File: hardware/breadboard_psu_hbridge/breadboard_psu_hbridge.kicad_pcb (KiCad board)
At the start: 2 copper layers, 51.7 x 45.7 mm, 52 parts, among them J1 USB_B_Micro, J2 Conn_01x02, J3 Conn_01x02, U1 74LS132, U2 LM4871MX_NOPB, U3 LM2733YMF, U4 ZXBM5210-S

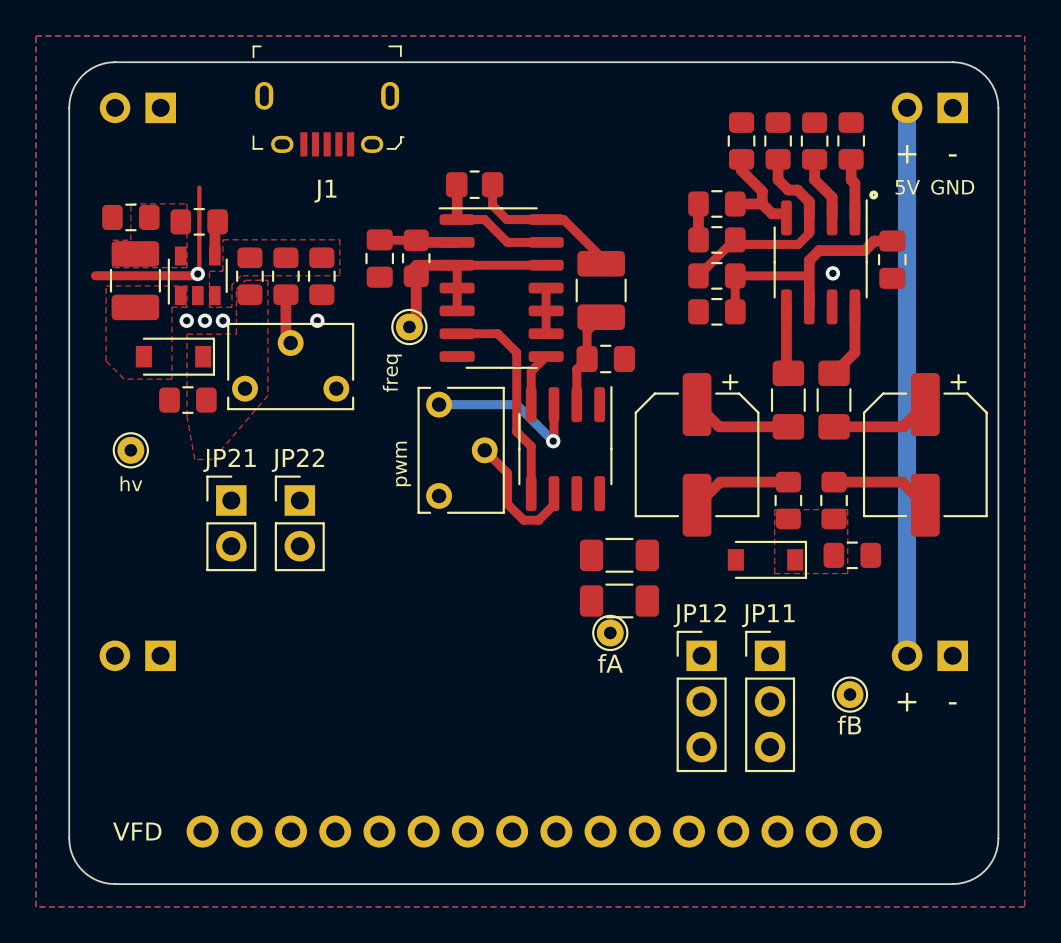
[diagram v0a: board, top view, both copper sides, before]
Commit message: hw: finished h-bridge psu test board
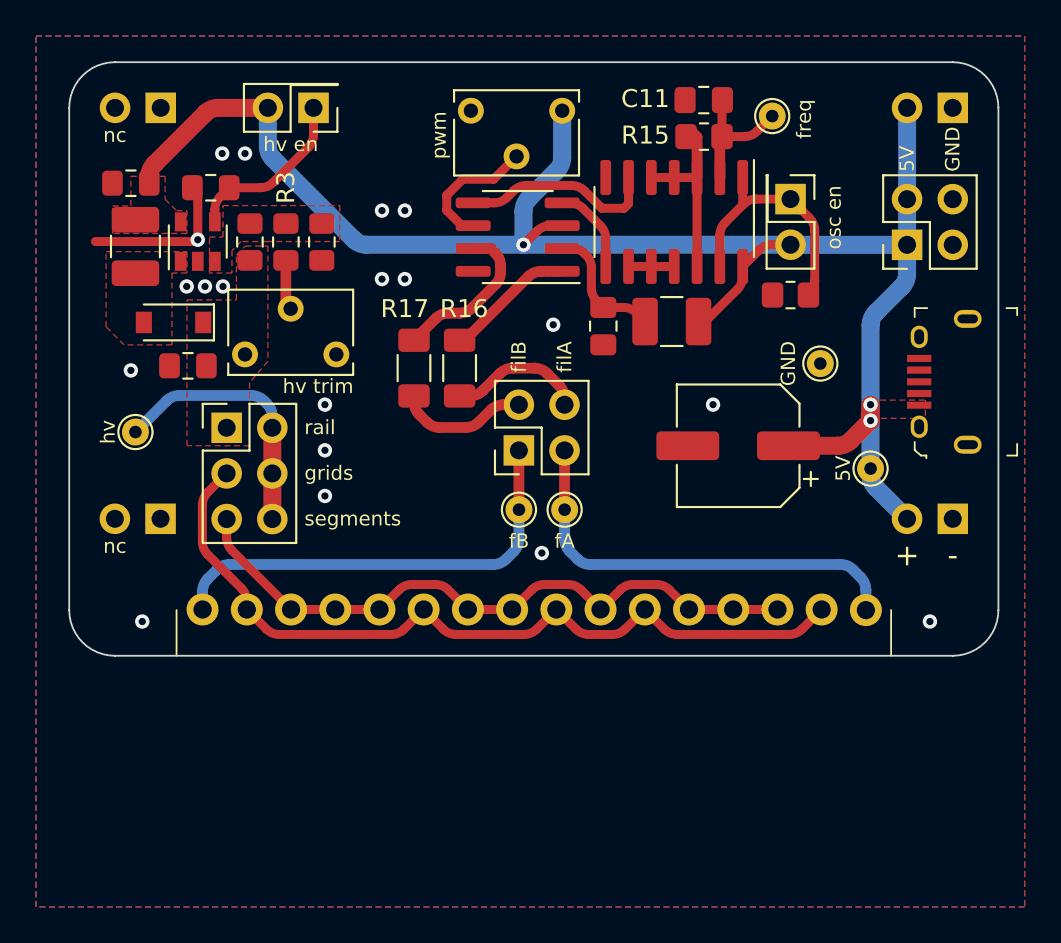
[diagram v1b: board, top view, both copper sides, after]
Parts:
- removed C10, C5: 1µF, Capacitor_SMD:C_0805_2012Metric_Pad1.15x1.40mm_HandSolder
- removed C6: 10µF, Capacitor_SMD:C_0805_2012Metric_Pad1.18x1.45mm_HandSolder
- removed C7, C8: 47µF, Capacitor_SMD:CP_Elec_6.3x5.9
- removed C9: 100nF, Capacitor_SMD:C_0805_2012Metric_Pad1.15x1.40mm_HandSolder
- removed D2: 3.3V, Diode_SMD:D_SOD-123
- removed JP11, JP12: Jumper_3_Bridged12, Connector_PinHeader_2.54mm:PinHeader_1x03_P2.54mm_Vertical
- removed JP21, JP22: Jumper_2_Bridged, Connector_PinHeader_2.54mm:PinHeader_1x02_P2.54mm_Vertical
- removed R10, R11: 12Ω 0.25W, Resistor_SMD:R_1206_3216Metric_Pad1.42x1.75mm_HandSolder
- removed R12, R13: 220Ω, Resistor_SMD:R_0805_2012Metric_Pad1.15x1.40mm_HandSolder
- removed R5, R6, R7, R9: 10kΩ, Resistor_SMD:R_0805_2012Metric_Pad1.15x1.40mm_HandSolder
- removed R8: 2.2kΩ, Resistor_SMD:R_0805_2012Metric_Pad1.15x1.40mm_HandSolder
- removed REF** (x2): PinHeader_1x02_P2.54mm_Vertical, Connector_PinHeader_2.54mm:PinHeader_1x02_P2.54mm_Vertical
- removed U2: LM4871MX_NOPB, Package_SO:SOIC-8_3.9x4.9mm_P1.27mm
- removed VFD: IVL2-7_5-singleSide, extra_libraries:IVL2-7_5-singleSide
- added A1: 2021, extra:AHOI, B.Cu at (127.8, 64.8)
- added J2: PWR Header, Connector_PinHeader_2.54mm:PinHeader_2x02_P2.54mm_Vertical, F.Cu at (137.3, 50.2)
- added J3: HV Jumper, Connector_PinHeader_2.54mm:PinHeader_2x03_P2.54mm_Vertical, F.Cu at (99.5, 60.3)
- added J31: Breadboard NC, Connector_PinHeader_2.54mm:PinHeader_1x02_P2.54mm_Vertical, B.Cu at (95.8, 42.5)
- added J32: Breadboard NC, Connector_PinHeader_2.54mm:PinHeader_1x02_P2.54mm_Vertical, B.Cu at (95.8, 65.4)
- added J4: Filament Jumper, Connector_PinHeader_2.54mm:PinHeader_2x02_P2.54mm_Vertical, F.Cu at (115.7, 61.6)
- added J5: Filament EN, Connector_PinHeader_2.54mm:PinHeader_2x01_P2.54mm_Vertical, F.Cu at (130.8, 47.6)
- added J6: HV EN, Connector_PinHeader_2.54mm:PinHeader_2x01_P2.54mm_Vertical, F.Cu at (104.3, 42.5)
- added TP1: 5V, TestPoint:TestPoint_THTPad_D1.5mm_Drill0.7mm, F.Cu at (135.3, 62.6)
- added TP4: GND, TestPoint:TestPoint_THTPad_D1.5mm_Drill0.7mm, F.Cu at (132.5, 56.8)
- added VFD1: IVL2-5_7, extra:IVL2-7_5-singleSide, F.Cu at (155.8, 102.5)
- C4: value 10nF -> 47µF; footprint Capacitor_SMD:C_0805_2012Metric_Pad1.15x1.40mm_HandSolder -> Capacitor_SMD:CP_Elec_6.3x5.9
- J21: renamed from J3; value Conn_01x02 -> Breadboard Rail
- J22: renamed from J2; value Conn_01x02 -> Breadboard Rail
- R14: value 2.7kΩ -> 10kΩ
- moved J1 35.5 mm to (138.0, 57.8), turned to 90 degrees
- moved TP3 23.3 mm to (129.8, 43.0), turned to 90 degrees
- moved TP11 21.1 mm to (115.7, 64.9)
- moved C11 20.1 mm to (126.0, 42.1), turned to 180 degrees
- moved R14 18.6 mm to (130.8, 53.0)
- moved RV1 17.7 mm to (118.1, 42.7), turned to 0 degrees
- moved R15 17.4 mm to (126.0, 44.1), turned to 180 degrees
- moved R17 17.3 mm to (109.9, 57.0), turned to 90 degrees
- moved C4 17.0 mm to (127.9, 61.3), turned to 180 degrees
- moved R16 13.7 mm to (112.4, 57.0), turned to 90 degrees
- moved U4 12.1 mm to (115.6, 49.7), turned to 180 degrees
- moved U1 10.3 mm to (124.3, 48.9), turned to -90 degrees
- moved J21 7.62 mm to (139.8, 65.4)
- moved TP12 7.31 mm to (118.3, 64.9)
- moved L2 4.29 mm to (124.2, 54.4), turned to 180 degrees
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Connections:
- C4 pad 1: Net-(C4-Pad1) -> /5V
- J1 pad 2: Net-(J1-Pad2) -> unconnected-(J1-Pad2)
- J1 pad 3: Net-(J1-Pad3) -> unconnected-(J1-Pad3)
- J1 pad 4: Net-(J1-Pad4) -> unconnected-(J1-Pad4)
- R1 pad 1: /5V -> Net-(U3-Pad4)
- R1 pad 2: /~{HV_SHDN} -> GND
- R14 pad 1: /5V -> /H_EN
- R14 pad 2: /H_SHDN -> GND
- R15 pad 2: Net-(R15-Pad2) -> Net-(U1-Pad12)
- TP2 pad 1: /HV -> /HV_Jumper
- TP3 pad 1: Net-(R15-Pad2) -> Net-(C11-Pad1)
- U1 pad 1: /H_SHDN -> /H_EN
- U1 pad 12: Net-(R15-Pad2) -> Net-(U1-Pad12)
- U1 pad 13: /H_SHDN -> /H_EN
- U1 pad 3: Net-(R15-Pad2) -> Net-(U1-Pad12)
- U1 pad 4: Net-(R15-Pad2) -> Net-(U1-Pad12)
- U1 pad 5: Net-(R15-Pad2) -> Net-(U1-Pad12)
- U3 pad 4: /~{HV_SHDN} -> Net-(U3-Pad4)
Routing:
- net /HV_Grids: track 0.00 -> 45.2 mm
- net /HV_Segments: track 0.00 -> 36.7 mm
- net /5V: track 62.6 -> 98.0 mm, vias 1 -> 3
- net /FIL_B: track 0.00 -> 25.0 mm
- net /FIL_A: track 0.00 -> 24.3 mm
- net /HV_Jumper: track 0.00 -> 14.7 mm
- net /H_EN: track 0.00 -> 14.1 mm
- net Net-(R15-Pad2): track 13.1 -> 0.00 mm
- net Net-(R5-Pad2): track 12.5 -> 0.00 mm
- net Net-(U1-Pad12): track 0.00 -> 10.1 mm
- net Net-(U3-Pad4): track 0.00 -> 9.72 mm
- net Net-(R17-Pad2): track 0.00 -> 8.95 mm
- net /FIL_H_A: track 0.00 -> 7.58 mm
- net /FIL_H_B: track 0.00 -> 7.33 mm
- net Net-(R16-Pad2): track 0.00 -> 7.25 mm
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- removed copper zone on F.Cu, net Net-(C10-Pad1)
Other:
- board size 51.7 x 45.7 mm -> 51.7 x 33 mm
- board text added: "VFD PSU HB"
- board text added: "filA"
- board text added: "filB"
- board text added: "grids"
- board text added: "hv en"
- board text added: "hv trim"
- board text added: "nc"
- board text added: "osc en"
- board text added: "rail"
- board text added: "segments"
- board text removed: "Breadboard VFD PSU"
- board text removed: "Breadboard VFD PSU v1.0 partly based on a design by rolo 2020 ansemjo"

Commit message: hw: tweak breadboard psu for fabrication
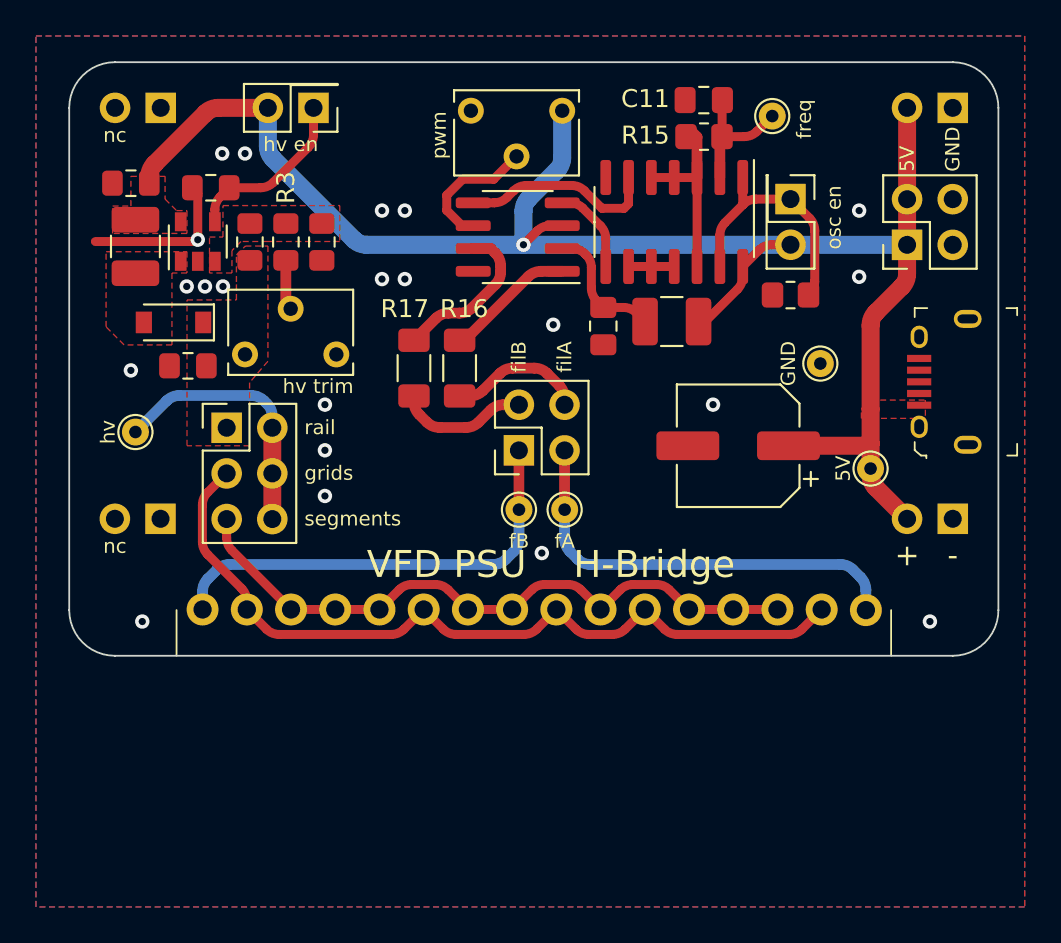
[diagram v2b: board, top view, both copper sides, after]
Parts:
- moved A1 1.87 mm to (127.9, 62.9)
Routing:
- net /5V: track 98.0 -> 96.6 mm, vias 3 -> 1
- net GND: vias 19 -> 21
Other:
- board text added: "JLCJLCJLCJLC"
- board text added: "VFD PSU H-Bridge"
- board text removed: "VFD PSU HB"
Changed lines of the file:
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@@
   (paper "A4")
   (title_block
+    (title "Breadboard VFD PSU")
+    (date "2021-08-28")
     (rev "1")
   )
@@
   )
   (footprint "extra:AHOI" (layer "B.Cu")
-    (at 127.778 64.77 180)
+    (at 127.905 62.9078 180)
     (property "Sheetfile" "breadboard_psu_hbridge.kicad_sch")
     (property "Sheetname" "")
@@
       (effects (font (size 1 1) (thickness 0.15)) (justify mirror))
     )
-    (fp_text user "ansemjo" (at 4.1 2.54) (layer "B.SilkS")
+    (fp_text user "ansemjo" (at 4.1 2.54 180) (layer "B.SilkS")
       (effects (font (size 1 1) (thickness 0.15)) (justify mirror))
     )
@@
   (gr_arc (start 139.843 70.485) (end 139.843 73.025) (angle -90) (layer "Edge.Cuts") (width 0.1))
   (gr_arc (start 139.843 42.545) (end 142.383 42.545) (angle -90) (layer "Edge.Cuts") (width 0.1))
+  (gr_text "JLCJLCJLCJLC" (at 127.905 66.167) (layer "B.SilkS")
+    (effects (font (size 0.8 0.8) (thickness 0.1)) (justify mirror))
+  )
   (gr_text "-" (at 139.843 67.437) (layer "F.SilkS")
     (effects (font (size 1.2 1.2) (thickness 0.3)))
@@
     (effects (font (size 0.8 0.8) (thickness 0.1)))
   )
+  (gr_text "VFD PSU    H-Bridge" (at 117.491 67.945) (layer "F.SilkS")
+    (effects (font (size 1.5 1.5) (thickness 0.3)))
+  )
   (gr_text "hv en" (at 103.013 44.577) (layer "F.SilkS")
     (effects (font (size 0.8 0.8) (thickness 0.1)))
@@
   (gr_text "filA" (at 118.253 57.277 90) (layer "F.SilkS")
     (effects (font (size 0.8 0.8) (thickness 0.1)) (justify left))
-  )
-  (gr_text "VFD PSU HB" (at 127.143 66.675) (layer "F.Mask")
-    (effects (font (size 1.5 1.5) (thickness 0.3)))
   )
   (segment (start 97.846 49.881) (end 97.82099 49.85599) (width 0.25) (layer "F.Cu") (net 1))
@@
   (via (at 138.573 71.12) (size 0.8) (drill 0.4) (layers "F.Cu" "B.Cu") (free) (net 1))
   (via (at 99.203 45.085) (size 0.8) (drill 0.4) (layers "F.Cu" "B.Cu") (free) (net 1))
+  (via (at 134.636 51.943) (size 0.8) (drill 0.4) (layers "F.Cu" "B.Cu") (free) (net 1))
   (via (at 109.363 52.07) (size 0.8) (drill 0.4) (layers "F.Cu" "B.Cu") (free) (net 1))
   (via (at 94.758 71.12) (size 0.8) (drill 0.4) (layers "F.Cu" "B.Cu") (free) (net 1))
@@
   (via (at 117.618 54.61) (size 0.8) (drill 0.4) (layers "F.Cu" "B.Cu") (free) (net 1))
   (via (at 109.363 48.26) (size 0.8) (drill 0.4) (layers "F.Cu" "B.Cu") (free) (net 1))
+  (via (at 134.636 48.26) (size 0.8) (drill 0.4) (layers "F.Cu" "B.Cu") (free) (net 1))
   (via (at 94.123 57.15) (size 0.8) (drill 0.4) (layers "F.Cu" "B.Cu") (free) (net 1))
   (segment (start 102.746 53.454) (end 103.013 53.721) (width 0.6) (layer "F.Cu") (net 3))
@@
   (segment (start 103.013 51.298) (end 102.746 51.031) (width 0.5) (layer "F.Cu") (net 3))
   (segment (start 128.159 51.994256) (end 128.159 51.37) (width 0.5) (layer "F.Cu") (net 5))
-  (segment (start 135.271 59.944) (end 135.271 59.055) (width 1) (layer "F.Cu") (net 5))
   (segment (start 127.866107 52.637893) (end 126.072 54.432) (width 0.5) (layer "F.Cu") (net 5))
   (segment (start 128.159 51.37) (end 128.159 51.930786) (width 0.5) (layer "F.Cu") (net 5))
   (segment (start 98.982214 42.545) (end 101.743 42.545) (width 1) (layer "F.Cu") (net 5))
   (segment (start 126.072 54.432) (end 125.7015 54.432) (width 0.5) (layer "F.Cu") (net 5))
-  (segment (start 130.705 61.341) (end 133.459786 61.341) (width 1) (layer "F.Cu") (net 5))
-  (segment (start 134.166893 61.048107) (end 135.271 59.944) (width 1) (layer "F.Cu") (net 5))
+  (segment (start 135.563893 53.936107) (end 137.010107 52.489893) (width 1) (layer "F.Cu") (net 5))
+  (segment (start 137.303 65.405) (end 135.563893 63.665893) (width 1) (layer "F.Cu") (net 5))
   (segment (start 128.159 51.37) (end 129.076107 50.452893) (width 0.5) (layer "F.Cu") (net 5))
   (segment (start 118.118 49.098) (end 117.438214 49.098) (width 0.5) (layer "F.Cu") (net 5))
+  (segment (start 135.271 62.958786) (end 135.271 61.214) (width 1) (layer "F.Cu") (net 5))
+  (segment (start 137.303 51.782786) (end 137.303 50.165) (width 1) (layer "F.Cu") (net 5))
+  (segment (start 135.271 61.214) (end 135.271 59.309) (width 1) (layer "F.Cu") (net 5))
+  (segment (start 130.705 61.341) (end 135.144 61.341) (width 1) (layer "F.Cu") (net 5))
+  (segment (start 135.144 61.341) (end 135.271 61.214) (width 1) (layer "F.Cu") (net 5))
+  (segment (start 135.271 59.309) (end 135.271 54.643214) (width 1) (layer "F.Cu") (net 5))
   (segment (start 116.731107 49.390893) (end 115.962 50.16) (width 0.5) (layer "F.Cu") (net 5))
   (segment (start 95.440893 45.672107) (end 98.275107 42.837893) (width 1) (layer "F.Cu") (net 5))
   (segment (start 129.783214 50.16) (end 130.818 50.16) (width 0.5) (layer "F.Cu") (net 5))
   (segment (start 95.148 46.736) (end 95.148 46.379214) (width 1) (layer "F.Cu") (net 5))
-  (via (at 135.271 59.055) (size 0.8) (drill 0.4) (layers "F.Cu" "B.Cu") (net 5))
+  (segment (start 137.303 50.165) (end 137.303 42.545) (width 1) (layer "F.Cu") (net 5))
   (via (at 115.962 50.16) (size 0.8) (drill 0.4) (layers "F.Cu" "B.Cu") (net 5))
-  (via (at 135.271 59.944) (size 0.8) (drill 0.4) (layers "F.Cu" "B.Cu") (net 5))
   (arc (start 128.159 51.930786) (mid 128.08288 52.313469) (end 127.866107 52.637893) (width 0.5) (layer "F.Cu") (net 5))
   (arc (start 98.982214 42.545) (mid 98.599531 42.62112) (end 98.275107 42.837893) (width 1) (layer "F.Cu") (net 5))
+  (arc (start 135.563893 63.665893) (mid 135.34712 63.34147) (end 135.271 62.958786) (width 1) (layer "F.Cu") (net 5))
   (arc (start 95.148 46.379214) (mid 95.22412 45.996531) (end 95.440893 45.672107) (width 1) (layer "F.Cu") (net 5))
   (arc (start 129.076107 50.452893) (mid 129.40053 50.23612) (end 129.783214 50.16) (width 0.5) (layer "F.Cu") (net 5))
-  (arc (start 134.166893 61.048107) (mid 133.84247 61.26488) (end 133.459786 61.341) (width 1) (layer "F.Cu") (net 5))
+  (arc (start 135.271 54.643214) (mid 135.34712 54.26053) (end 135.563893 53.936107) (width 1) (layer "F.Cu") (net 5))
+  (arc (start 137.010107 52.489893) (mid 137.22688 52.16547) (end 137.303 51.782786) (width 1) (layer "F.Cu") (net 5))
   (arc (start 117.438214 49.098) (mid 117.055531 49.17412) (end 116.731107 49.390893) (width 0.5) (layer "F.Cu") (net 5))
   (segment (start 115.962 50.16) (end 107.232214 50.16) (width 1) (layer "B.Cu") (net 5))
-  (segment (start 135.563893 63.665893) (end 137.303 65.405) (width 1) (layer "B.Cu") (net 5))
-  (segment (start 135.271 54.643214) (end 135.271 59.309) (width 1) (layer "B.Cu") (net 5))
   (segment (start 106.525107 49.867107) (end 102.035893 45.377893) (width 1) (layer "B.Cu") (net 5))
   (segment (start 118.118 42.705) (end 118.118 45.313786) (width 1) (layer "B.Cu") (net 5))
   (segment (start 117.825107 46.020893) (end 116.254893 47.591107) (width 1) (layer "B.Cu") (net 5))
   (segment (start 130.818 50.16) (end 115.962 50.16) (width 1) (layer "B.Cu") (net 5))
-  (segment (start 137.303 50.165) (end 137.303 51.782786) (width 1) (layer "B.Cu") (net 5))
-  (segment (start 135.271 59.944) (end 135.271 59.309) (width 1) (layer "B.Cu") (net 5))
   (segment (start 130.823 50.165) (end 130.818 50.16) (width 1) (layer "B.Cu") (net 5))
-  (segment (start 135.271 59.944) (end 135.271 62.958786) (width 1) (layer "B.Cu") (net 5))
-  (segment (start 137.010107 52.489893) (end 135.563893 53.936107) (width 1) (layer "B.Cu") (net 5))
   (segment (start 137.303 50.165) (end 130.823 50.165) (width 1) (layer "B.Cu") (net 5))
   (segment (start 115.962 48.298214) (end 115.962 50.16) (width 1) (layer "B.Cu") (net 5))
   (segment (start 101.743 44.670786) (end 101.743 42.545) (width 1) (layer "B.Cu") (net 5))
-  (segment (start 137.303 50.165) (end 137.303 42.545) (width 1) (layer "B.Cu") (net 5))
-  (arc (start 135.563893 63.665893) (mid 135.34712 63.34147) (end 135.271 62.958786) (width 1) (layer "B.Cu") (net 5))
-  (arc (start 137.010107 52.489893) (mid 137.22688 52.16547) (end 137.303 51.782786) (width 1) (layer "B.Cu") (net 5))
-  (arc (start 135.563893 53.936107) (mid 135.34712 54.26053) (end 135.271 54.643214) (width 1) (layer "B.Cu") (net 5))
   (arc (start 118.118 45.313786) (mid 118.04188 45.696469) (end 117.825107 46.020893) (width 1) (layer "B.Cu") (net 5))
   (arc (start 106.525107 49.867107) (mid 106.84953 50.08388) (end 107.232214 50.16) (width 1) (layer "B.Cu") (net 5))

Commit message: hw: update breadboard hbridge psu to kicad 6
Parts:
- added kibuzzard-61E14426: G***, kibuzzard-61E14426, F.Cu at (116.7, 67.7)
- C1, C2, C3: footprint Capacitor_SMD:C_0805_2012Metric_Pad1.15x1.40mm_HandSolder -> Capacitor_SMD:C_0805_2012Metric_Pad1.18x1.45mm_HandSolder
- J1: footprint digikey-footprints:USB_Micro_B_Female_10118194-0001LF -> Connector_USB:USB_Micro-B_Amphenol_10118194_Horizontal
- R1, R2, R3: footprint Resistor_SMD:R_0805_2012Metric_Pad1.15x1.40mm_HandSolder -> Resistor_SMD:R_0805_2012Metric_Pad1.20x1.40mm_HandSolder
- moved J1 1.33 mm to (139.3, 57.8)
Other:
- board text removed: "VFD PSU H-Bridge"
